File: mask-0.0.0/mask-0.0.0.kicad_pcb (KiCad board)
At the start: 2 copper layers, 165 x 113 mm, 106 parts, among them J1 Conn_02x05_Counter_Clockwise, J2 Conn_ARM_JTAG_SWD_10, J3 USB_C_Receptacle_USB2.0, J4 USB_C_Receptacle_USB2.0, Q1 IRLML2502, SW1 SW_Push, SW10 SW_Push, SW11 SW_Push, SW12 SW_Push, SW13 SW_Push, SW13_1 SW_Push, SW14 SW_Push, SW15 SW_Push, SW16 SW_Push, SW17 SW_Push, SW18 SW_Push, SW19 SW_Push, SW2 SW_Push, SW20 SW_Push, SW20_1 SW_Push, SW21 SW_Push, SW22 SW_Push, SW23 SW_Push, SW24 SW_Push, SW25 SW_Push, SW26 SW_Push, SW27 SW_Push, SW27_1 SW_Push, SW28 SW_Push, SW29 SW_Push, SW3 SW_Push, SW30 SW_Push, SW31 SW_Push, SW32 SW_Push, SW33 SW_Push, SW34 SW_Push, SW35 SW_Push, SW4 SW_Push, SW5 SW_Push, SW6 SW_Push, SW7 SW_Push, SW8 SW_Push, SW9 SW_Push, U1 NORA-B10x, U2 MCP1703A-3302_SOT23

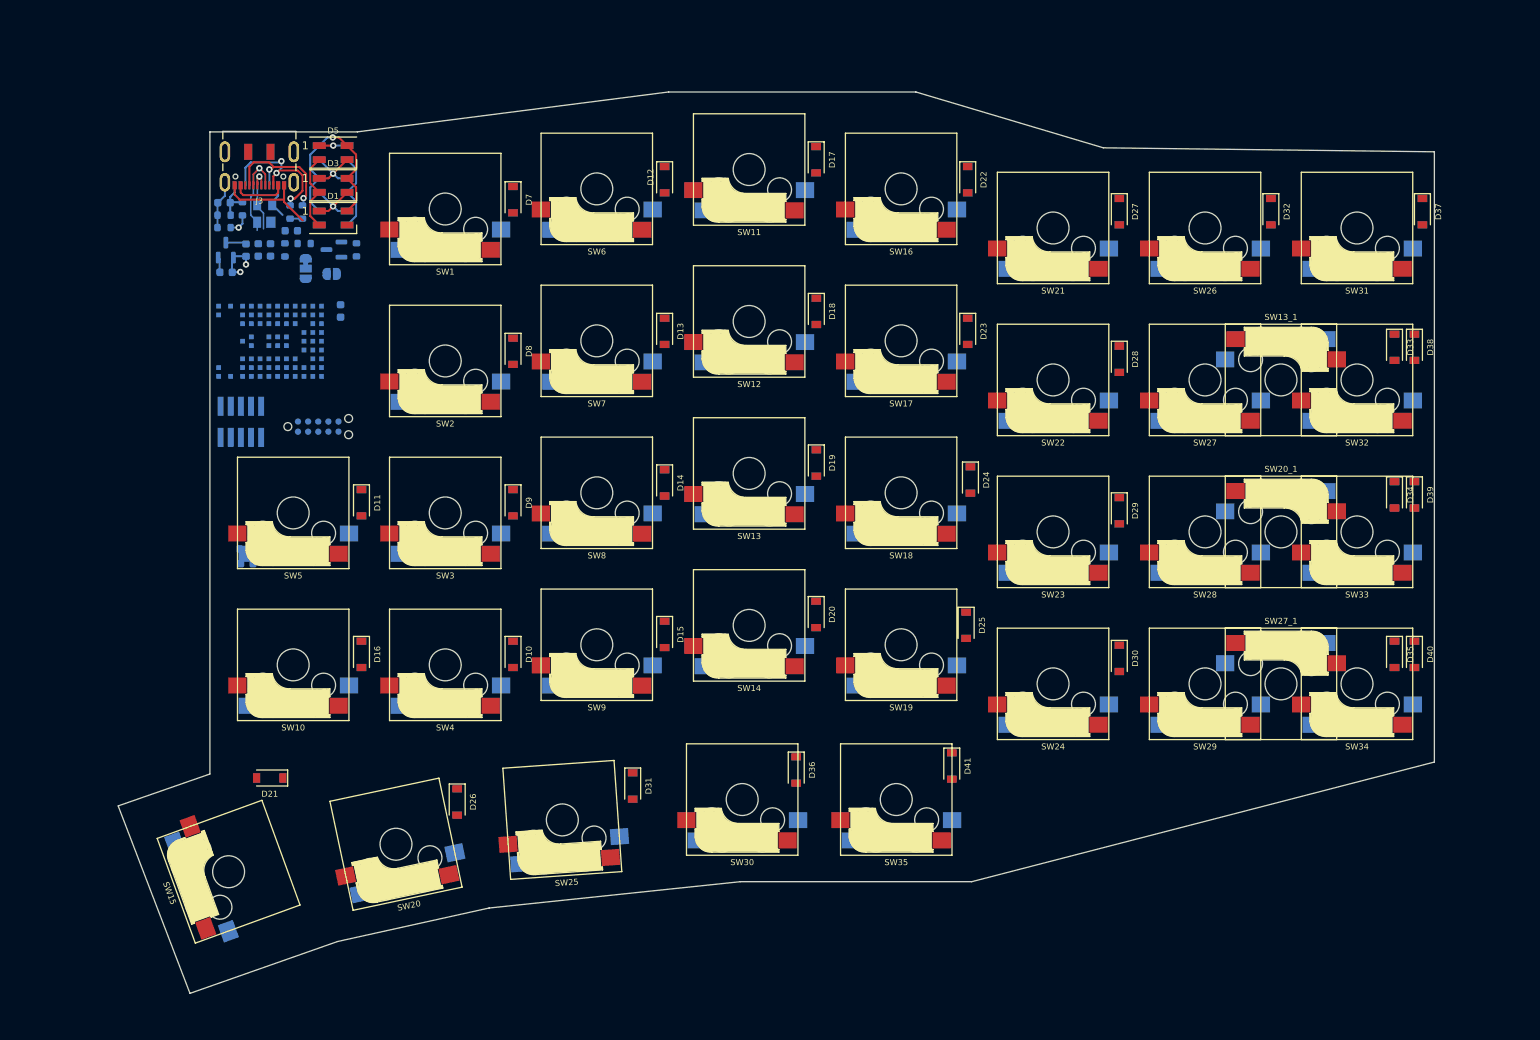
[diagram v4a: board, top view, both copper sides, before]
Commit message: mask-0.0.0: begin of matrix routing
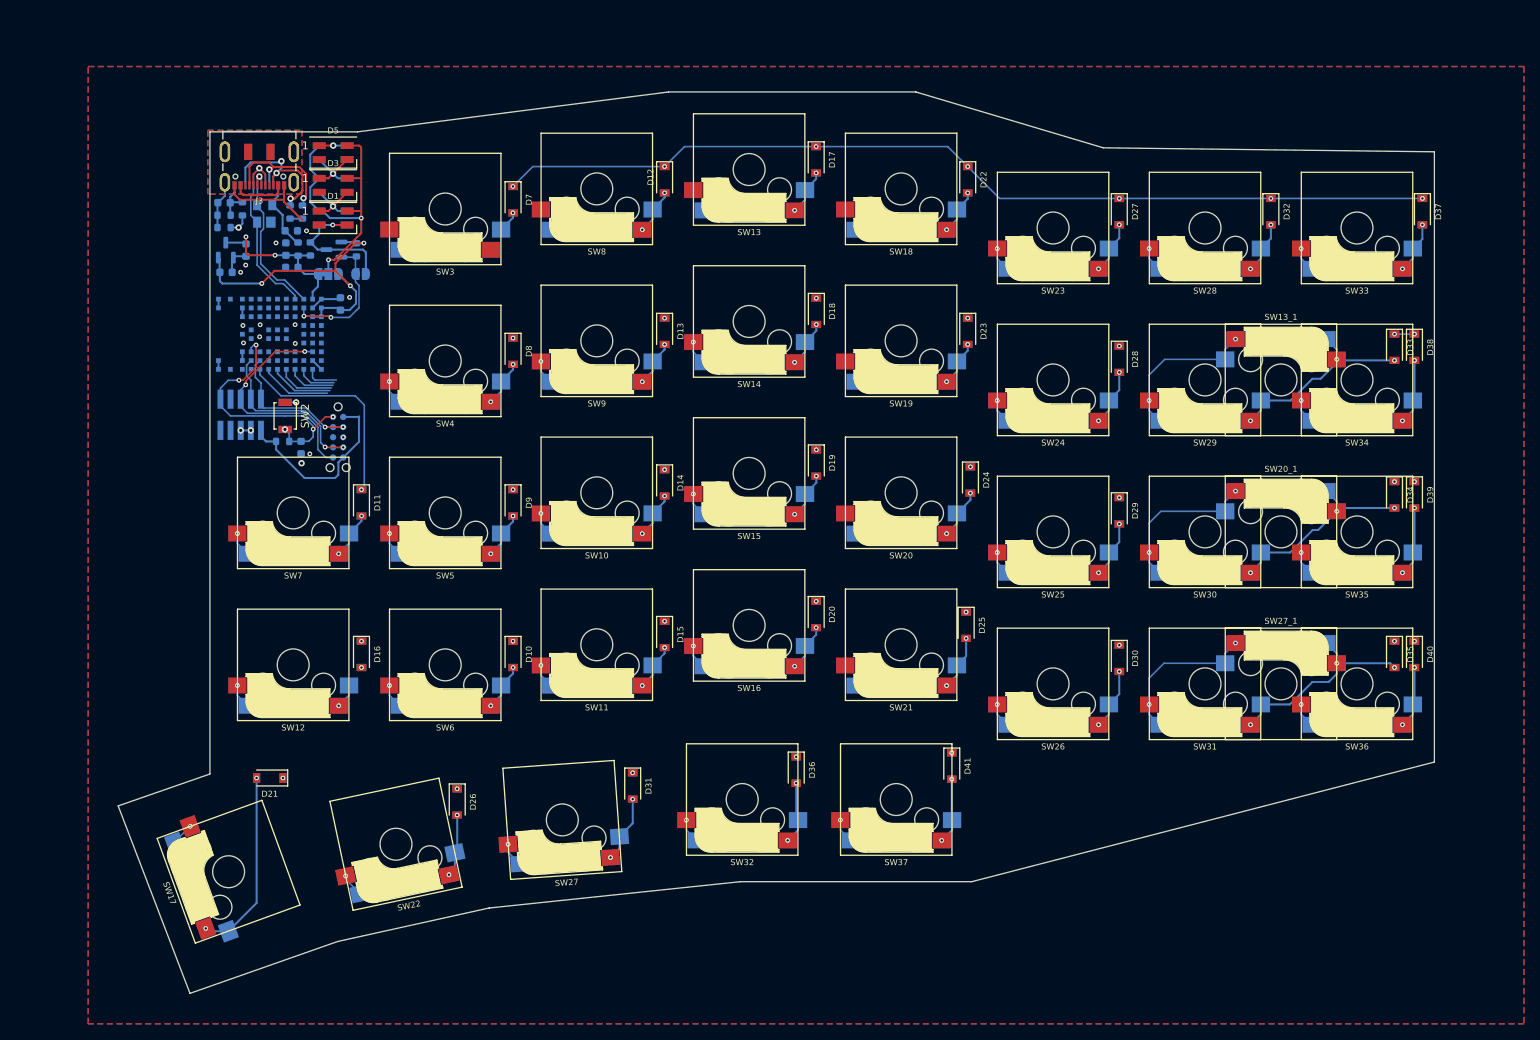
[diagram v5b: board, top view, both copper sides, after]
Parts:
- added SW1: SW_Push, Button_Switch_SMD:SW_SPST_B3U-1000P, B.Cu at (49.9, 98.1)
- added SW2: SW_Push, Button_Switch_SMD:SW_SPST_B3U-1000P, F.Cu at (49.9, 98.1)
- moved C4 16.1 mm to (51.9, 102.1), turned to -90 degrees
- moved R2 14.2 mm to (49.6, 101.3), turned to 0 degrees
- moved C8 4.75 mm to (50.8, 79.5), turned to 180 degrees
- moved JP1 3.63 mm to (59.4, 80.3), turned to 180 degrees
- moved JP2 2.92 mm to (55.4, 80.3), turned to 0 degrees
- moved J1 2.83 mm to (56.6, 100.8), turned to -90 degrees
- moved C7 1.92 mm to (50.0, 77.2), turned to 90 degrees
- moved FB3 1.65 mm to (51.5, 77.2)
- moved R3 1.04 mm to (53.1, 77.2), turned to 90 degrees
- moved C1 0.88 mm to (56.9, 84.1)
- moved J2 0.88 mm to (44.4, 98.0), turned to 90 degrees
- moved U1 0.88 mm to (49.0, 87.9)
- renumbered R2 to R1, R1 to R2, SW8 to SW10, SW9 to SW11, SW10 to SW12, SW11 to SW13, SW12 to SW14, SW13 to SW15, SW14 to SW16, SW15 to SW17, SW16 to SW18, SW17 to SW19, SW18 to SW20, SW19 to SW21, SW20 to SW22, SW21 to SW23, SW22 to SW24, SW23 to SW25, SW24 to SW26, SW25 to SW27, SW26 to SW28, SW27 to SW29, SW1 to SW3, SW28 to SW30, SW29 to SW31, SW30 to SW32, SW31 to SW33, SW32 to SW34, SW33 to SW35, SW34 to SW36, SW35 to SW37, SW2 to SW4, SW3 to SW5, SW4 to SW6, SW5 to SW7, SW6 to SW8, SW7 to SW9
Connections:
- U1 pad A2: unconnected-(U1-PadA2) -> ROW1
- U1 pad A3: unconnected-(U1-PadA3) -> ROW0
- U1 pad A4: unconnected-(U1-PadA4) -> COL2
- U1 pad A5: unconnected-(U1-PadA5) -> COL0
- U1 pad B1: unconnected-(U1-PadB1) -> ROW2
- U1 pad B4: unconnected-(U1-PadB4) -> COL1
- U1 pad C1: unconnected-(U1-PadC1) -> ROW3
- U1 pad C8: unconnected-(U1-PadC8) -> LED
- U1 pad D1: unconnected-(U1-PadD1) -> COL3
- U1 pad E1: unconnected-(U1-PadE1) -> COL4
- U1 pad F1: unconnected-(U1-PadF1) -> COL5
- U1 pad G1: unconnected-(U1-PadG1) -> COL6
- U1 pad H1: unconnected-(U1-PadH1) -> ROW4
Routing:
- net ROW0: track 0.00 -> 118.8 mm, vias 0 -> 7
- net COL5: track 0.00 -> 73.6 mm, vias 0 -> 8
- net +3V3: track 1.83 -> 64.7 mm, vias 0 -> 3
- net RESET: track 0.00 -> 34.0 mm, vias 0 -> 5
- net SWO: track 0.00 -> 29.2 mm, vias 0 -> 2
- net ROW4: track 0.00 -> 26.1 mm, vias 0 -> 7
- net Net-(D35-Pad2): track 0.00 -> 26.0 mm, vias 0 -> 3
- net Net-(D33-Pad2): track 0.00 -> 25.3 mm, vias 0 -> 3
- net Net-(D34-Pad2): track 0.00 -> 25.2 mm, vias 0 -> 3
- net COL6: track 0.00 -> 24.3 mm, vias 0 -> 5
- net Net-(D21-Pad2): track 0.62 -> 24.3 mm, vias 0 -> 2
- net COL4: track 0.00 -> 22.6 mm, vias 0 -> 5
- net SWDCLK: track 0.00 -> 21.1 mm, vias 0 -> 2
- net +5V: track 2.36 -> 21.3 mm, vias 0 -> 2
- net SWDIO: track 0.00 -> 17.6 mm, vias 0 -> 2
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- added copper zone on B.Cu, net /Usb/USB_SHIELD
- added copper zone on F.Cu, net /Usb/USB_SHIELD
- added copper zone on B.Cu, net GND
- added copper zone on F.Cu, net GND

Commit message: mask-0.0.0: routed
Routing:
- net COL6: track 24.3 -> 319.0 mm, vias 5 -> 7
- net COL3: track 9.02 -> 237.0 mm, vias 1 -> 7
- net COL5: track 73.6 -> 271.1 mm, vias 8 -> 10
- net COL4: track 22.6 -> 219.7 mm, vias 5 -> 7
- net COL2: track 12.1 -> 190.1 mm, vias 4 -> 11
- net ROW3: track 4.96 -> 177.0 mm, vias 7 -> 14
- net ROW2: track 4.15 -> 157.2 mm, vias 7 -> 14
- net ROW1: track 2.50 -> 147.0 mm, vias 7 -> 14
- net ROW4: track 26.1 -> 157.8 mm
- net COL1: track 12.3 -> 140.2 mm, vias 4 -> 9
- net COL0: track 12.3 -> 95.2 mm, vias 4 -> 7
- net ROW0: track 118.8 -> 157.1 mm, vias 7 -> 9
- net +3V3: track 64.7 -> 78.2 mm, vias 3 -> 5
- net /Usb/GND_USB: track 20.2 -> 25.0 mm, vias 0 -> 2
- net Net-(D7-Pad2): track 2.72 -> 5.80 mm, vias 1 -> 2
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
